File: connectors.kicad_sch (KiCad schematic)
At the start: 3 parts, among them J1 0436500200, J2 0430450200, J3 IPS1-110-01-L-D

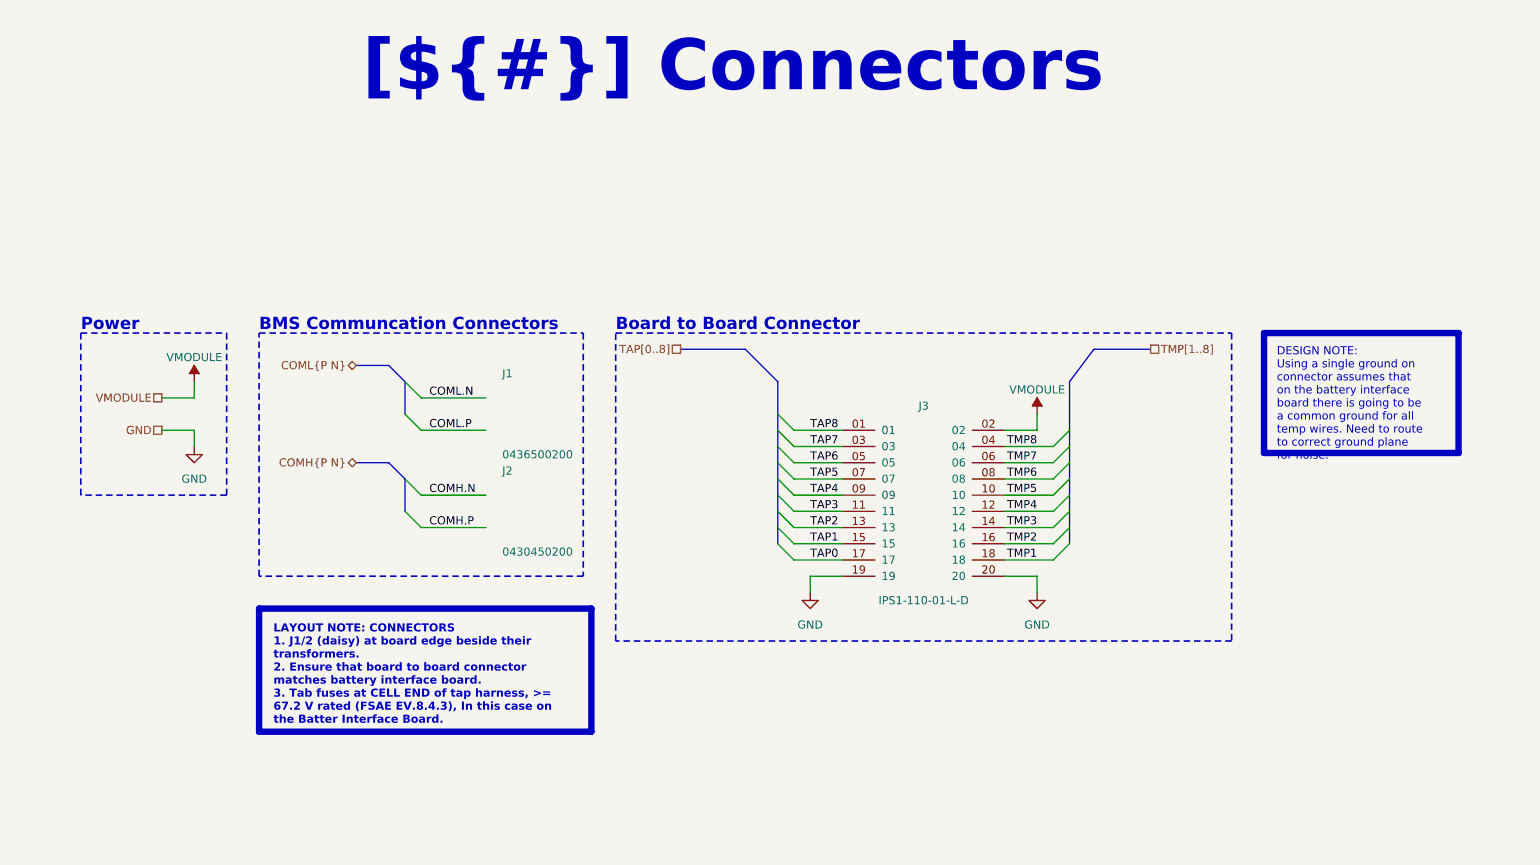
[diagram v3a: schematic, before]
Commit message: PCB[Test Points, Mechanical, Silk]: Finalized Mounting Points, Added Testpoints with adjecent silkscreen labels. SCH[Test Points, Notes]: Added/Updated notes for all pages, cleaned up errors spelling ect.
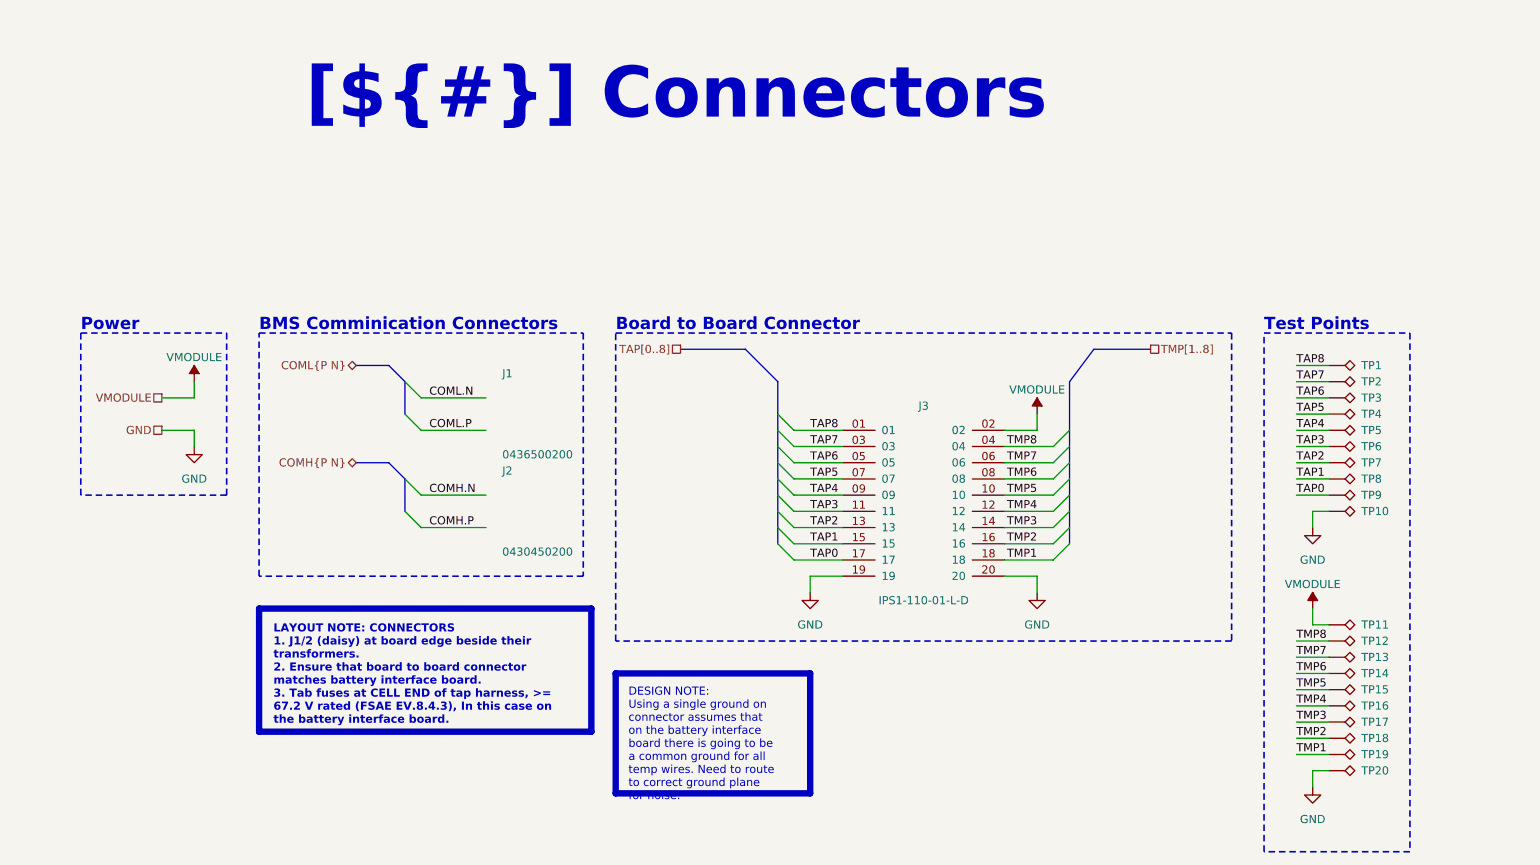
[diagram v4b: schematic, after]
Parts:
- added TP1, TP10, TP11, TP12, TP13, TP14, TP15, TP16, TP17, TP18, TP19, TP2, TP20, TP3, TP4, TP5, TP6, TP7, TP8, TP9: TestPoint_Alt, TestPoint:TestPoint_Pad_1.0x1.0mm, symbol Connector:TestPoint_Alt
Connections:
- net GND: now also TP10.1, TP20.1
- net TAP0: now also TP9.1
- net TAP1: now also TP8.1
- net TAP2: now also TP7.1
- net TAP3: now also TP6.1
- net TAP4: now also TP5.1
- net TAP5: now also TP4.1
- net TAP6: now also TP3.1
- net TAP7: now also TP2.1
- net TAP8: now also TP1.1
- net TMP1: now also TP19.1
- net TMP2: now also TP18.1
- net TMP3: now also TP17.1
- net TMP4: now also TP16.1
- net TMP5: now also TP15.1
- net TMP6: now also TP14.1
- net TMP7: now also TP13.1
- net TMP8: now also TP12.1
- net VMODULE: now also TP11.1
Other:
- note added: "BMS Comminication Connectors"
- note added: "Test Points"
- note removed: "BMS Communcation Connectors"

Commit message: PCB[Trace Size, Testpad, Daisy]: Changed Bat Trace size FAT, Made test pads larger, small trace movement to clean up, daisy trace change. SCH[Notes]: Small notes changes.
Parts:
- TP1, TP10, TP11, TP12, TP13, TP14, TP15, TP16, TP17, TP18, TP19, TP2, TP20, TP3, TP4, TP5, TP6, TP7, TP8, TP9: footprint TestPoint:TestPoint_Pad_1.0x1.0mm -> TestPoint:TestPoint_Pad_1.5x1.5mm
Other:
- company: (none) -> ${COMPANY}
